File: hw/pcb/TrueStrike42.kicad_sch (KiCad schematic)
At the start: 154 parts, among them SW1 SW_Push, U1 ProMicro, U10 4053, U2 74HC4051, U3 74HC4051, U4 74HC4051, U5 74HC4051, U6 74HC4051, U7 74HC4051, U8 74HC4051, U9 74AHCT125

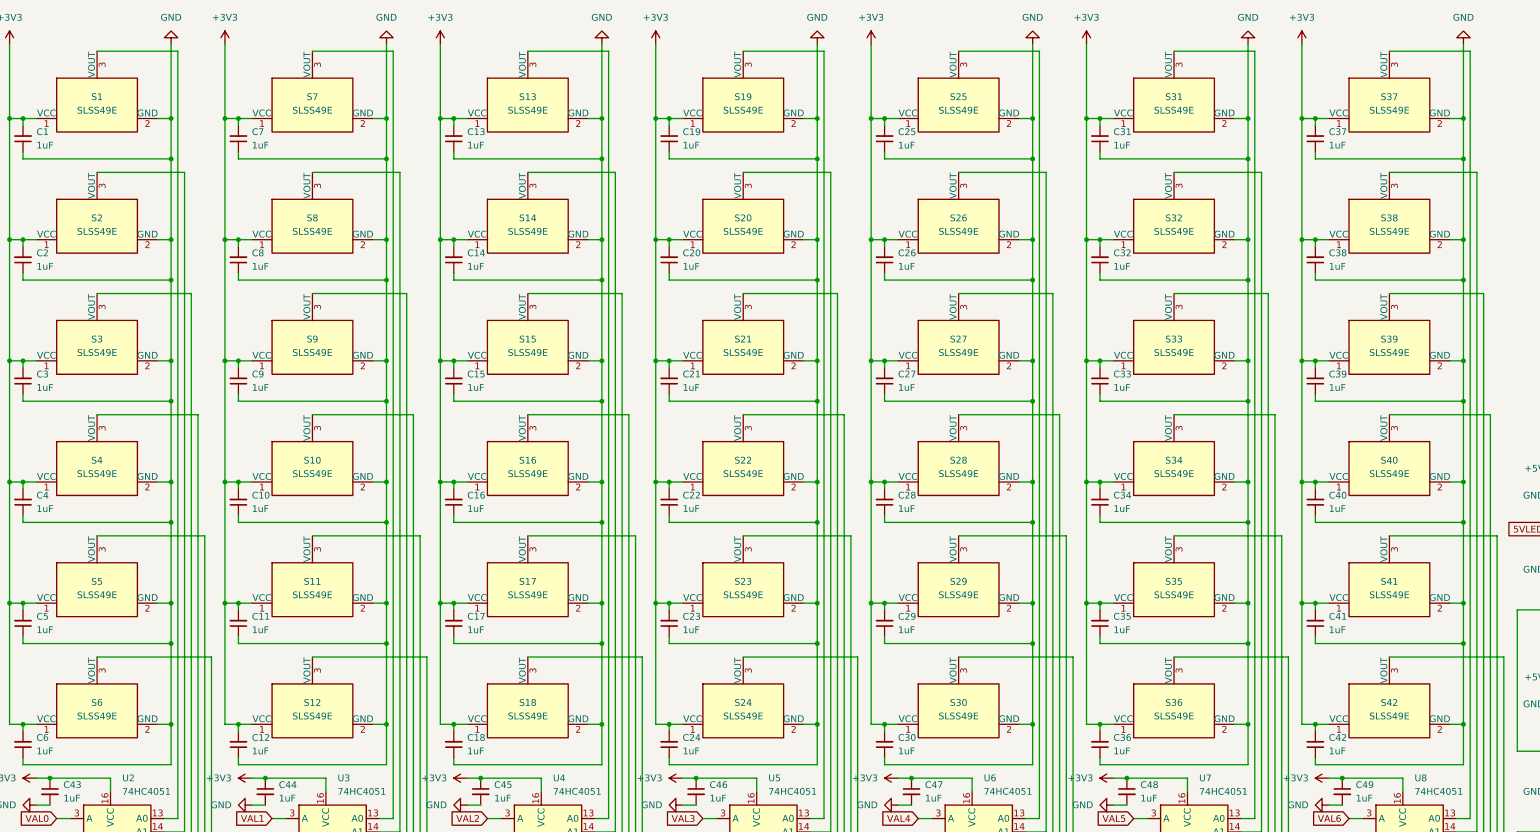
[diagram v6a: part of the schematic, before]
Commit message: Add logo, fixed wrong pinouts for sensors
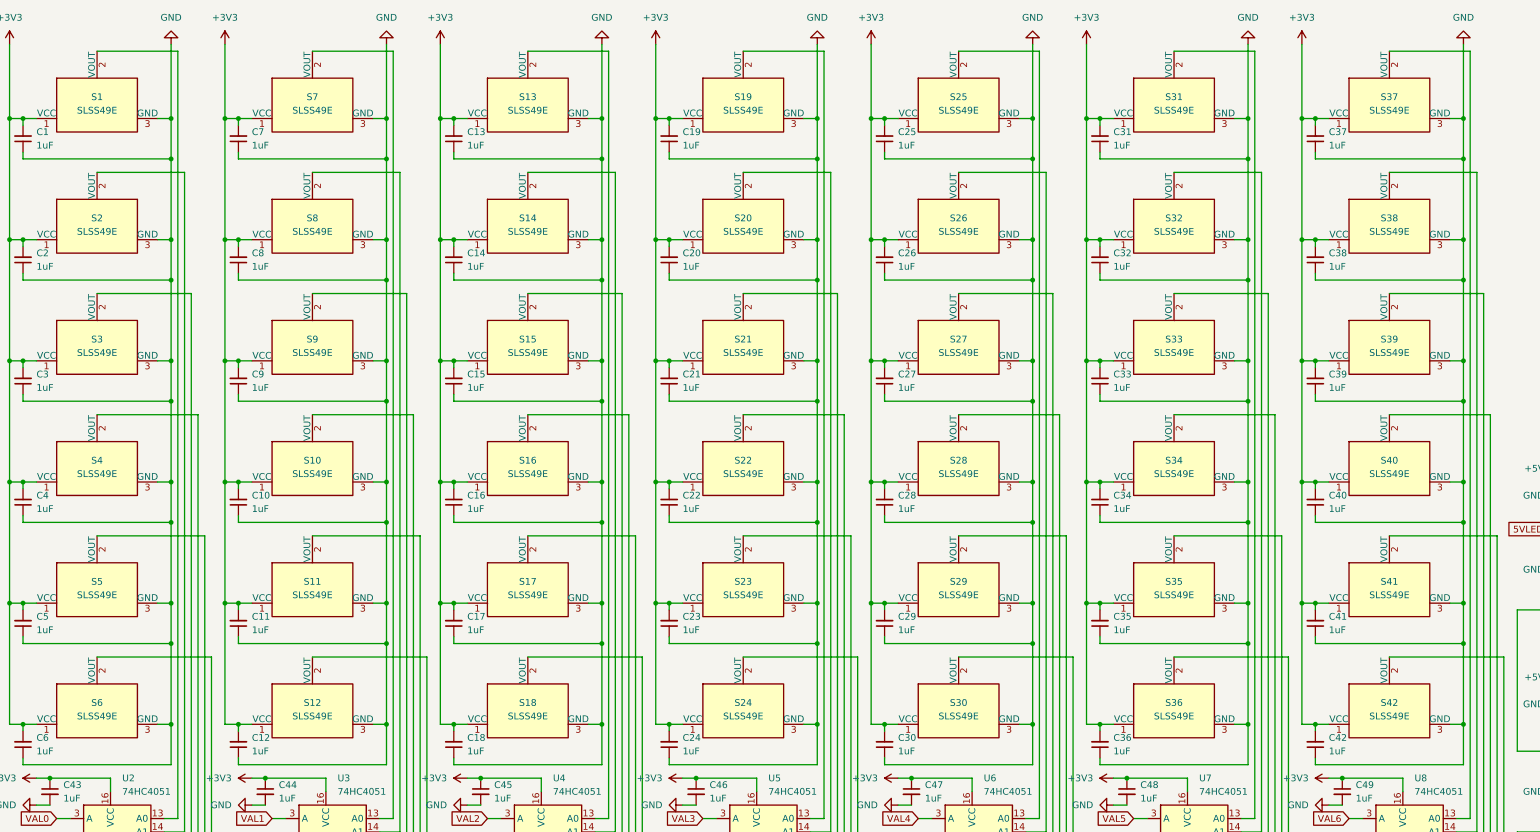
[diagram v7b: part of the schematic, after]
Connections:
- net GND: now also S1.3 (GND), S10.3 (GND), S11.3 (GND), S12.3 (GND), S13.3 (GND), S14.3 (GND), S15.3 (GND), S16.3 (GND), S17.3 (GND), S18.3 (GND), S19.3 (GND), S2.3 (GND), S20.3 (GND), S21.3 (GND), S22.3 (GND), S23.3 (GND), S24.3 (GND), S25.3 (GND), S26.3 (GND), S27.3 (GND), S28.3 (GND), S29.3 (GND), S3.3 (GND), S30.3 (GND), S31.3 (GND), S32.3 (GND), S33.3 (GND), S34.3 (GND), S35.3 (GND), S36.3 (GND), S37.3 (GND), S38.3 (GND), S39.3 (GND), S4.3 (GND), S40.3 (GND), S41.3 (GND), S42.3 (GND), S5.3 (GND), S6.3 (GND), S7.3 (GND), S8.3 (GND), S9.3 (GND); no longer S1.2 (GND), S10.2 (GND), S11.2 (GND), S12.2 (GND), S13.2 (GND), S14.2 (GND), S15.2 (GND), S16.2 (GND), S17.2 (GND), S18.2 (GND), S19.2 (GND), S2.2 (GND), S20.2 (GND), S21.2 (GND), S22.2 (GND), S23.2 (GND), S24.2 (GND), S25.2 (GND), S26.2 (GND), S27.2 (GND), S28.2 (GND), S29.2 (GND), S3.2 (GND), S30.2 (GND), S31.2 (GND), S32.2 (GND), S33.2 (GND), S34.2 (GND), S35.2 (GND), S36.2 (GND), S37.2 (GND), S38.2 (GND), S39.2 (GND), S4.2 (GND), S40.2 (GND), S41.2 (GND), S42.2 (GND), S5.2 (GND), S6.2 (GND), S7.2 (GND), S8.2 (GND), S9.2 (GND)
- net at U6.13 (A0): now also S25.2 (VOUT); no longer S25.3 (VOUT)
- net at U4.14 (A1): now also S14.2 (VOUT); no longer S14.3 (VOUT)
- net at U3.14 (A1): now also S8.2 (VOUT); no longer S8.3 (VOUT)
- net at U7.5 (A5): now also S36.2 (VOUT); no longer S36.3 (VOUT)
- net at U6.1 (A4): now also S29.2 (VOUT); no longer S29.3 (VOUT)
- net at U2.15 (A2): now also S3.2 (VOUT); no longer S3.3 (VOUT)
- net at U8.14 (A1): now also S38.2 (VOUT); no longer S38.3 (VOUT)
- net at U2.1 (A4): now also S5.2 (VOUT); no longer S5.3 (VOUT)
- net at U8.1 (A4): now also S41.2 (VOUT); no longer S41.3 (VOUT)
- net at U8.12 (A3): now also S40.2 (VOUT); no longer S40.3 (VOUT)
- net at U8.13 (A0): now also S37.2 (VOUT); no longer S37.3 (VOUT)
- net at U8.15 (A2): now also S39.2 (VOUT); no longer S39.3 (VOUT)
- net at U8.5 (A5): now also S42.2 (VOUT); no longer S42.3 (VOUT)
- net at U2.5 (A5): now also S6.2 (VOUT); no longer S6.3 (VOUT)
- net at U4.5 (A5): now also S18.2 (VOUT); no longer S18.3 (VOUT)
- net at U2.14 (A1): now also S2.2 (VOUT); no longer S2.3 (VOUT)
- net at U5.1 (A4): now also S23.2 (VOUT); no longer S23.3 (VOUT)
- net at U5.12 (A3): now also S22.2 (VOUT); no longer S22.3 (VOUT)
- net at U6.12 (A3): now also S28.2 (VOUT); no longer S28.3 (VOUT)
- net at U3.13 (A0): now also S7.2 (VOUT); no longer S7.3 (VOUT)
- net at U3.1 (A4): now also S11.2 (VOUT); no longer S11.3 (VOUT)
- net at U5.13 (A0): now also S19.2 (VOUT); no longer S19.3 (VOUT)
- net at U7.1 (A4): now also S35.2 (VOUT); no longer S35.3 (VOUT)
- net at U7.12 (A3): now also S34.2 (VOUT); no longer S34.3 (VOUT)
- net at U7.13 (A0): now also S31.2 (VOUT); no longer S31.3 (VOUT)
- net at U7.14 (A1): now also S32.2 (VOUT); no longer S32.3 (VOUT)
- net at U7.15 (A2): now also S33.2 (VOUT); no longer S33.3 (VOUT)
- net at U2.12 (A3): now also S4.2 (VOUT); no longer S4.3 (VOUT)
- net at U2.13 (A0): now also S1.2 (VOUT); no longer S1.3 (VOUT)
- net at U5.14 (A1): now also S20.2 (VOUT); no longer S20.3 (VOUT)
- net at U4.1 (A4): now also S17.2 (VOUT); no longer S17.3 (VOUT)
- net at U6.14 (A1): now also S26.2 (VOUT); no longer S26.3 (VOUT)
- net at U5.5 (A5): now also S24.2 (VOUT); no longer S24.3 (VOUT)
- net at U3.12 (A3): now also S10.2 (VOUT); no longer S10.3 (VOUT)
- net at U3.15 (A2): now also S9.2 (VOUT); no longer S9.3 (VOUT)
- net at U3.5 (A5): now also S12.2 (VOUT); no longer S12.3 (VOUT)
- net at U6.15 (A2): now also S27.2 (VOUT); no longer S27.3 (VOUT)
- net at U6.5 (A5): now also S30.2 (VOUT); no longer S30.3 (VOUT)
- net at U5.15 (A2): now also S21.2 (VOUT); no longer S21.3 (VOUT)
- net at U4.12 (A3): now also S16.2 (VOUT); no longer S16.3 (VOUT)
- net at U4.13 (A0): now also S13.2 (VOUT); no longer S13.3 (VOUT)
- net at U4.15 (A2): now also S15.2 (VOUT); no longer S15.3 (VOUT)
